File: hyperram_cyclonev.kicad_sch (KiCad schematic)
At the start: 61 parts, among them IC1 AP63205WU, IC2 TXB0108PWR, IC3 S26KL128SDABHI020, IC4 W25Q32JVSSIQ_TR, IC5 S27KL0641DABHI020, J1 ASP-122952-01, J2 HDMI_A, J3 1156915, J4 1156915, J5 Conn_02x06_Top_Bottom, J6 Conn_02x06_Top_Bottom, J7 Conn_02x06_Top_Bottom, J8 1156915, J9 1156915, Q1 BSS138, Q2 BSS138

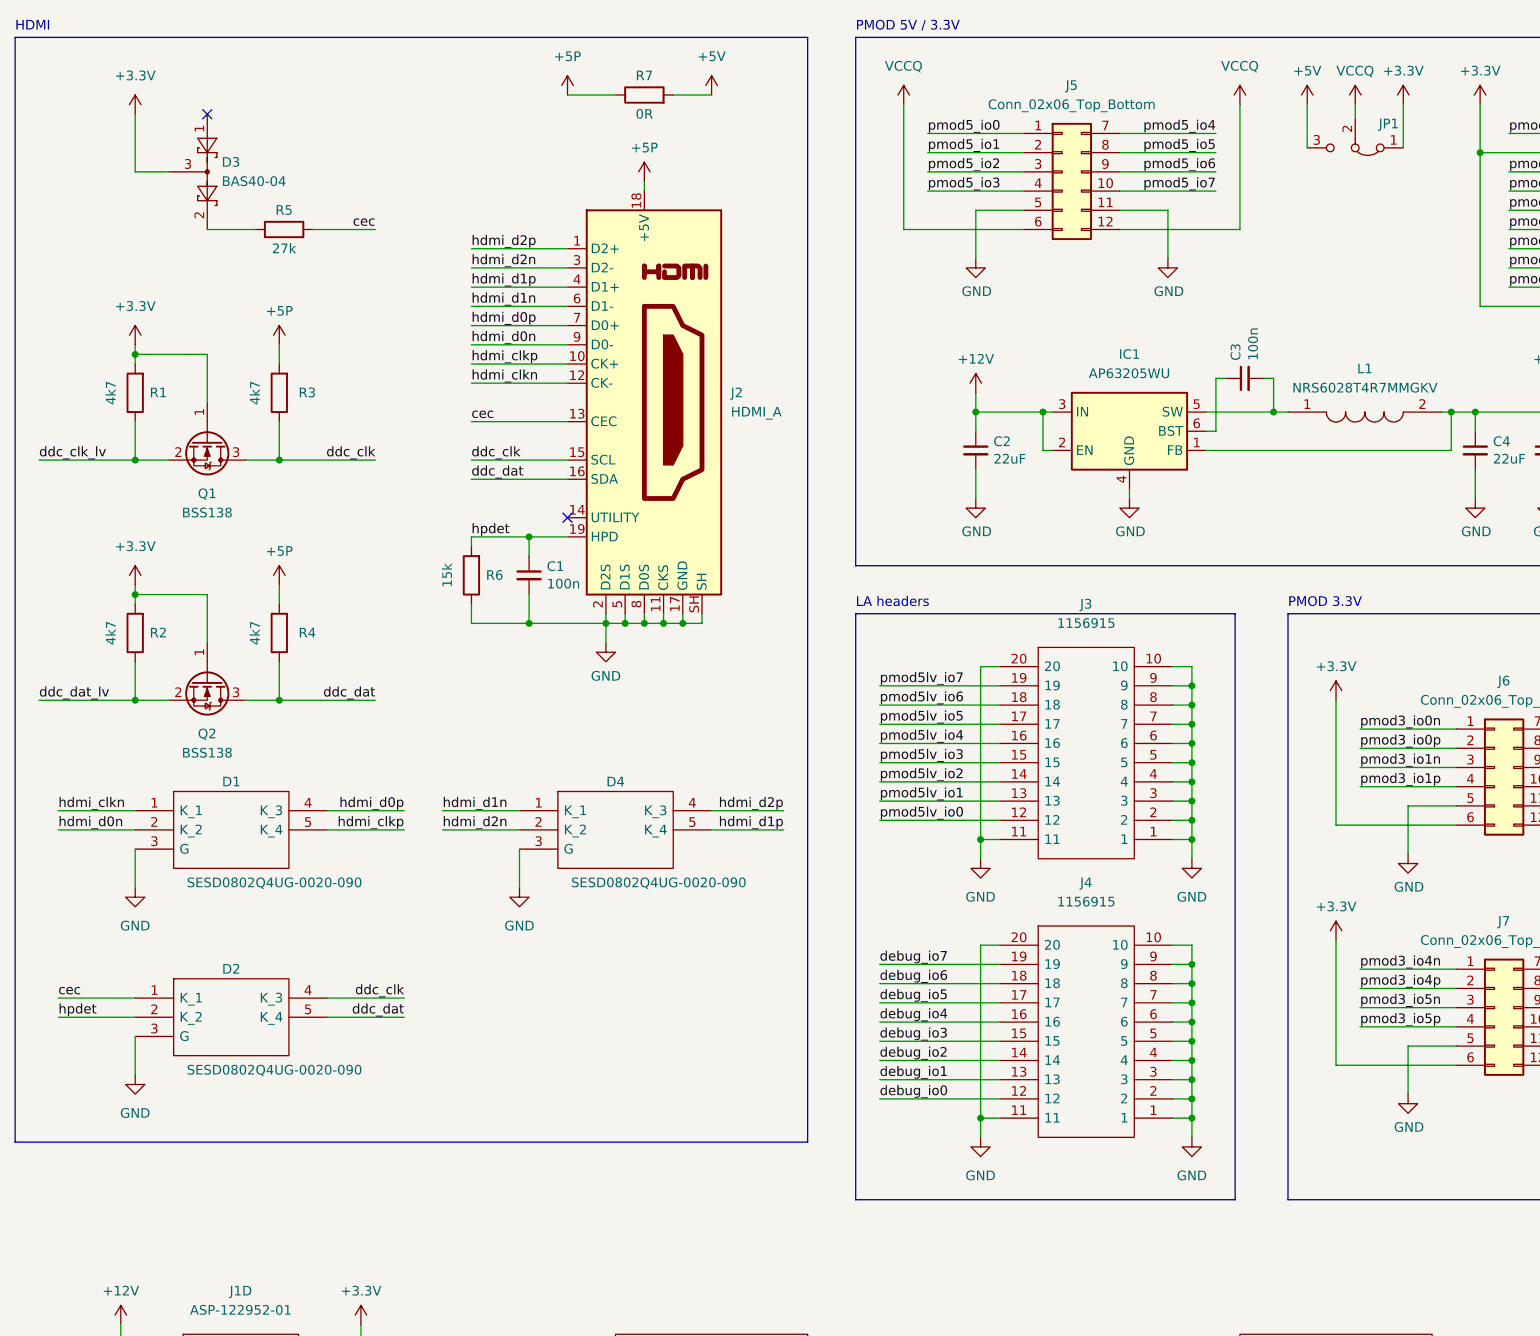
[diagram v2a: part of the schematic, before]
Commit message: Added 100nF capacitors in series for HDMI signals to get TMDS working with LVDS3 outputs on FPGA.
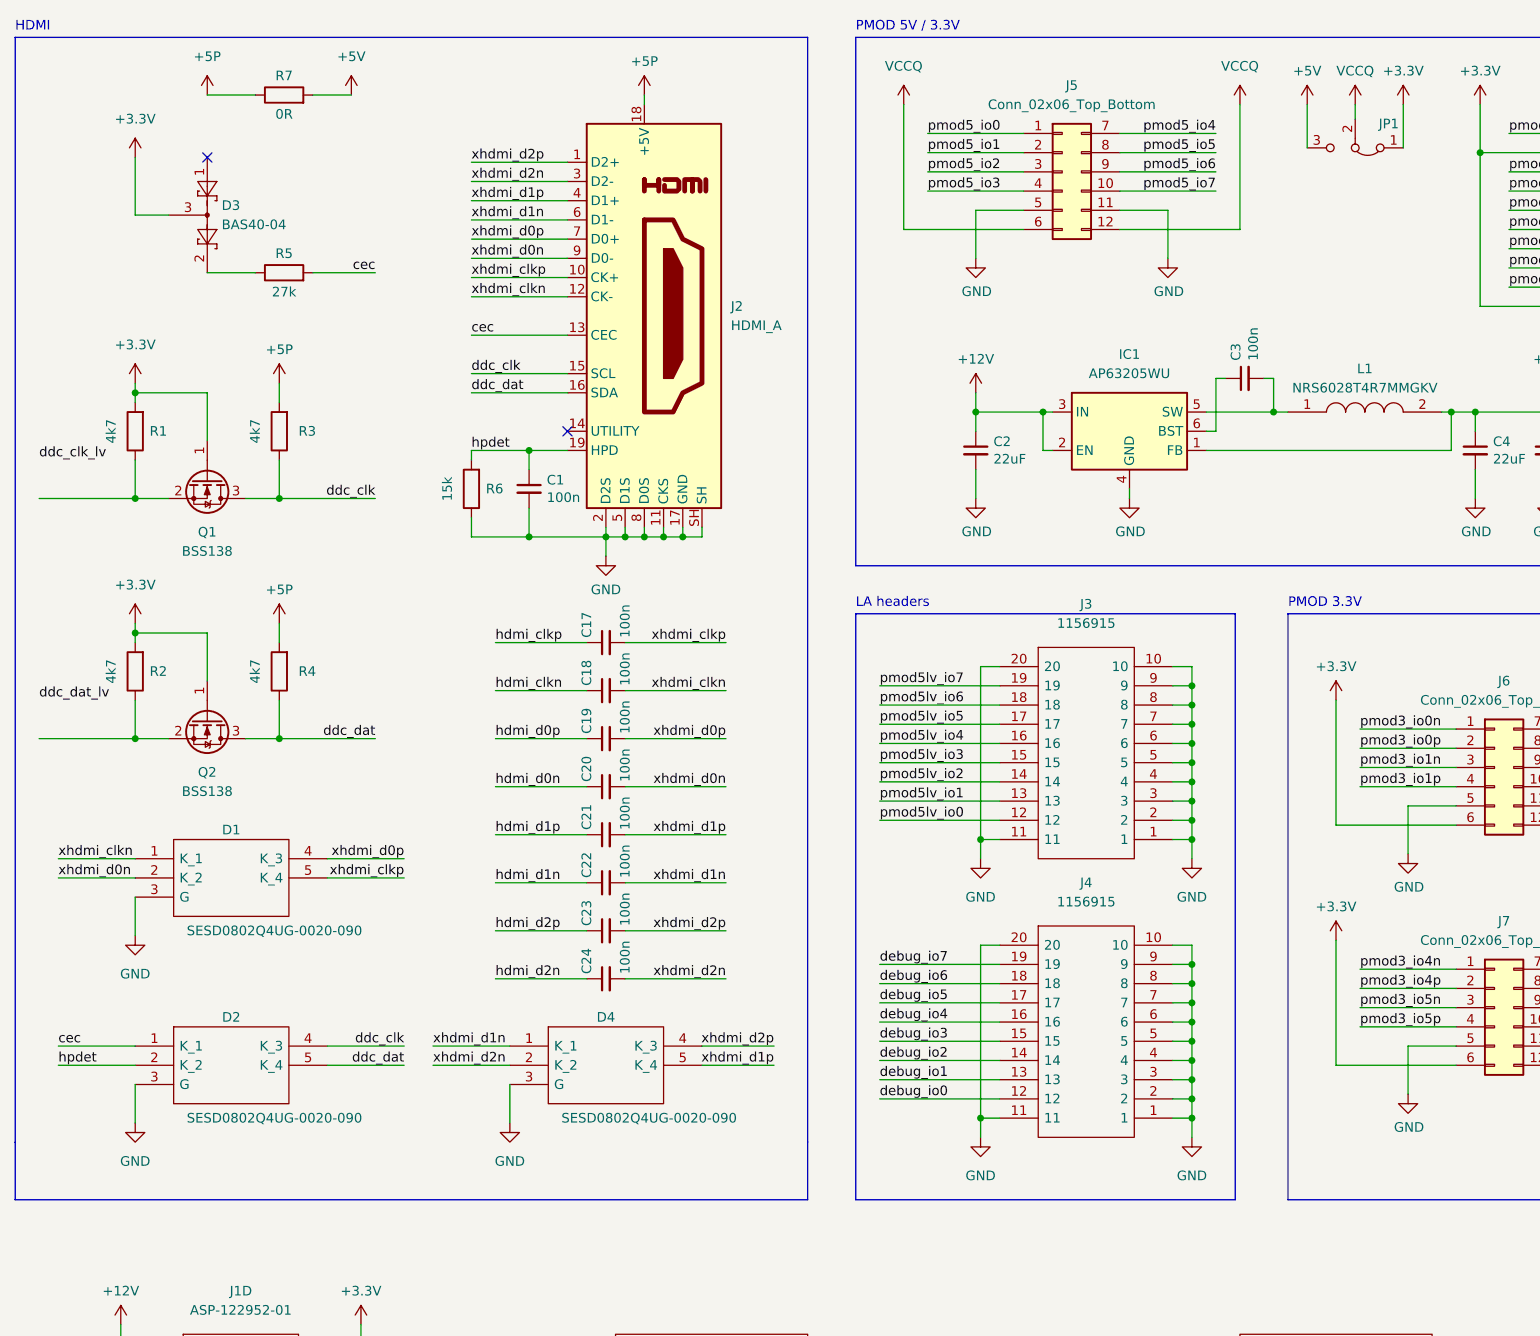
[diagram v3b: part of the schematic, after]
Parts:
- added C17, C18, C19, C20, C21, C22, C23, C24: 100n, Capacitor_SMD:C_0603_1608Metric_Pad1.08x0.95mm_HandSolder, symbol Device:C_Small
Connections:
- net ddc_clk_lv: no longer Q1.2 (S), R1.1
- net ddc_dat_lv: no longer Q2.2 (S), R2.1
- net hdmi_clkn: now also C18.1; no longer D1.1 (K_1), J2.12 (CK-)
- net hdmi_clkp: now also C17.1; no longer D1.5 (K_4), J2.10 (CK+)
- net hdmi_d0n: now also C20.1; no longer D1.2 (K_2), J2.9 (D0-)
- net hdmi_d0p: now also C19.1; no longer D1.4 (K_3), J2.7 (D0+)
- net hdmi_d1n: now also C22.1; no longer D4.1 (K_1), J2.6 (D1-)
- net hdmi_d1p: now also C21.1; no longer D4.5 (K_4), J2.4 (D1+)
- net hdmi_d2n: now also C24.1; no longer D4.2 (K_2), J2.3 (D2-)
- net hdmi_d2p: now also C23.1; no longer D4.4 (K_3), J2.1 (D2+)
- new net: Q1.2 (S), R1.1
- new net: Q2.2 (S), R2.1
- new net xhdmi_clkn: C18.2, D1.1 (K_1), J2.12 (CK-)
- new net xhdmi_clkp: C17.2, D1.5 (K_4), J2.10 (CK+)
- new net xhdmi_d0n: C20.2, D1.2 (K_2), J2.9 (D0-)
- new net xhdmi_d0p: C19.2, D1.4 (K_3), J2.7 (D0+)
- new net xhdmi_d1n: C22.2, D4.1 (K_1), J2.6 (D1-)
- new net xhdmi_d1p: C21.2, D4.5 (K_4), J2.4 (D1+)
- new net xhdmi_d2n: C24.2, D4.2 (K_2), J2.3 (D2-)
- new net xhdmi_d2p: C23.2, D4.4 (K_3), J2.1 (D2+)
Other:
- moved on the sheet: C1, D1, D2, D3, D4, J2, L1, Q1, Q2, R1, R2, R3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

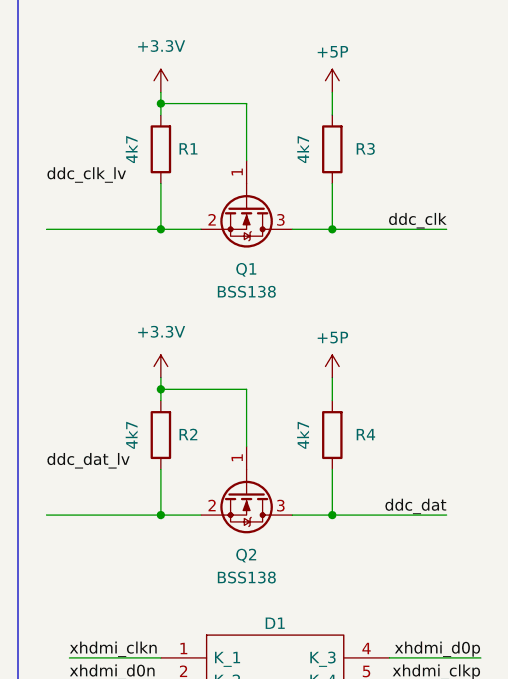
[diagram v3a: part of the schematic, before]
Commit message: Fixed 2 issues with unconnected signals.
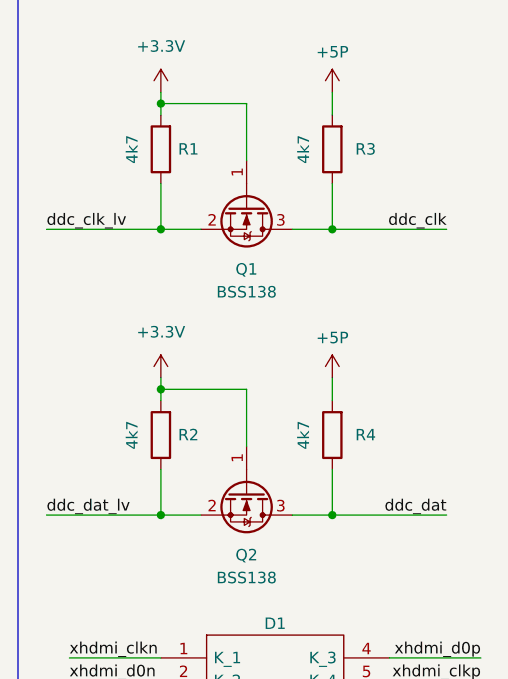
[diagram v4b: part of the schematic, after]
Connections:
- net ddc_clk_lv: now also Q1.2 (S), R1.1
- net ddc_dat_lv: now also Q2.2 (S), R2.1
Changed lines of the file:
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@@
     (effects (font (size 1.27 1.27)) (justify right bottom))
   )
-  (label "ddc_dat_lv" (at 19.05 106.68 0) (fields_autoplaced)
+  (label "ddc_dat_lv" (at 19.05 111.76 0) (fields_autoplaced)
     (effects (font (size 1.27 1.27)) (justify left bottom))
   )
@@
     (effects (font (size 1.27 1.27)) (justify left bottom))
   )
-  (label "ddc_clk_lv" (at 19.05 74.93 0) (fields_autoplaced)
+  (label "ddc_clk_lv" (at 19.05 80.01 0) (fields_autoplaced)
     (effects (font (size 1.27 1.27)) (justify left bottom))
   )
@@
     )
   )
-  (symbol (lib_id "hyperram_cyclonev:ASP-122952-01") (at 58.42 193.04 0) (unit 4)
+  (symbol (lib_name "ASP-122952-01_1") (lib_id "hyperram_cyclonev:ASP-122952-01") (at 58.42 193.04 0) (unit 4)
     (in_bom yes) (on_board yes) (dnp no) (fields_autoplaced)
     (property "Reference" "J1" (at 45.72 184.785 0)

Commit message: Fixed Schematics DRC warnings
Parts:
- Q1, Q2: footprint Package_TO_SOT_SMD:SOT-23_Handsoldering -> Package_TO_SOT_SMD:SOT-23
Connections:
- net GND: now also J3.12, J3.13, J3.14, J3.15, J3.16, J3.17, J3.18, J3.19; no longer J3.2, J3.3, J3.4, J3.5, J3.6, J3.7, J3.8, J3.9
- net pmod5lv_io0: now also J3.2; no longer J3.12
- net pmod5lv_io1: now also J3.3; no longer J3.13
- net pmod5lv_io2: now also J3.4; no longer J3.14
- net pmod5lv_io3: now also J3.5; no longer J3.15
- net pmod5lv_io4: now also J3.6; no longer J3.16
- net pmod5lv_io5: now also J3.7; no longer J3.17
- net pmod5lv_io6: now also J3.8; no longer J3.18
- net pmod5lv_io7: now also J3.9; no longer J3.19
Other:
- moved on the sheet: C2, C3, C4, C5, C6, C7, D1, D2, D3, IC1, J1D, J3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

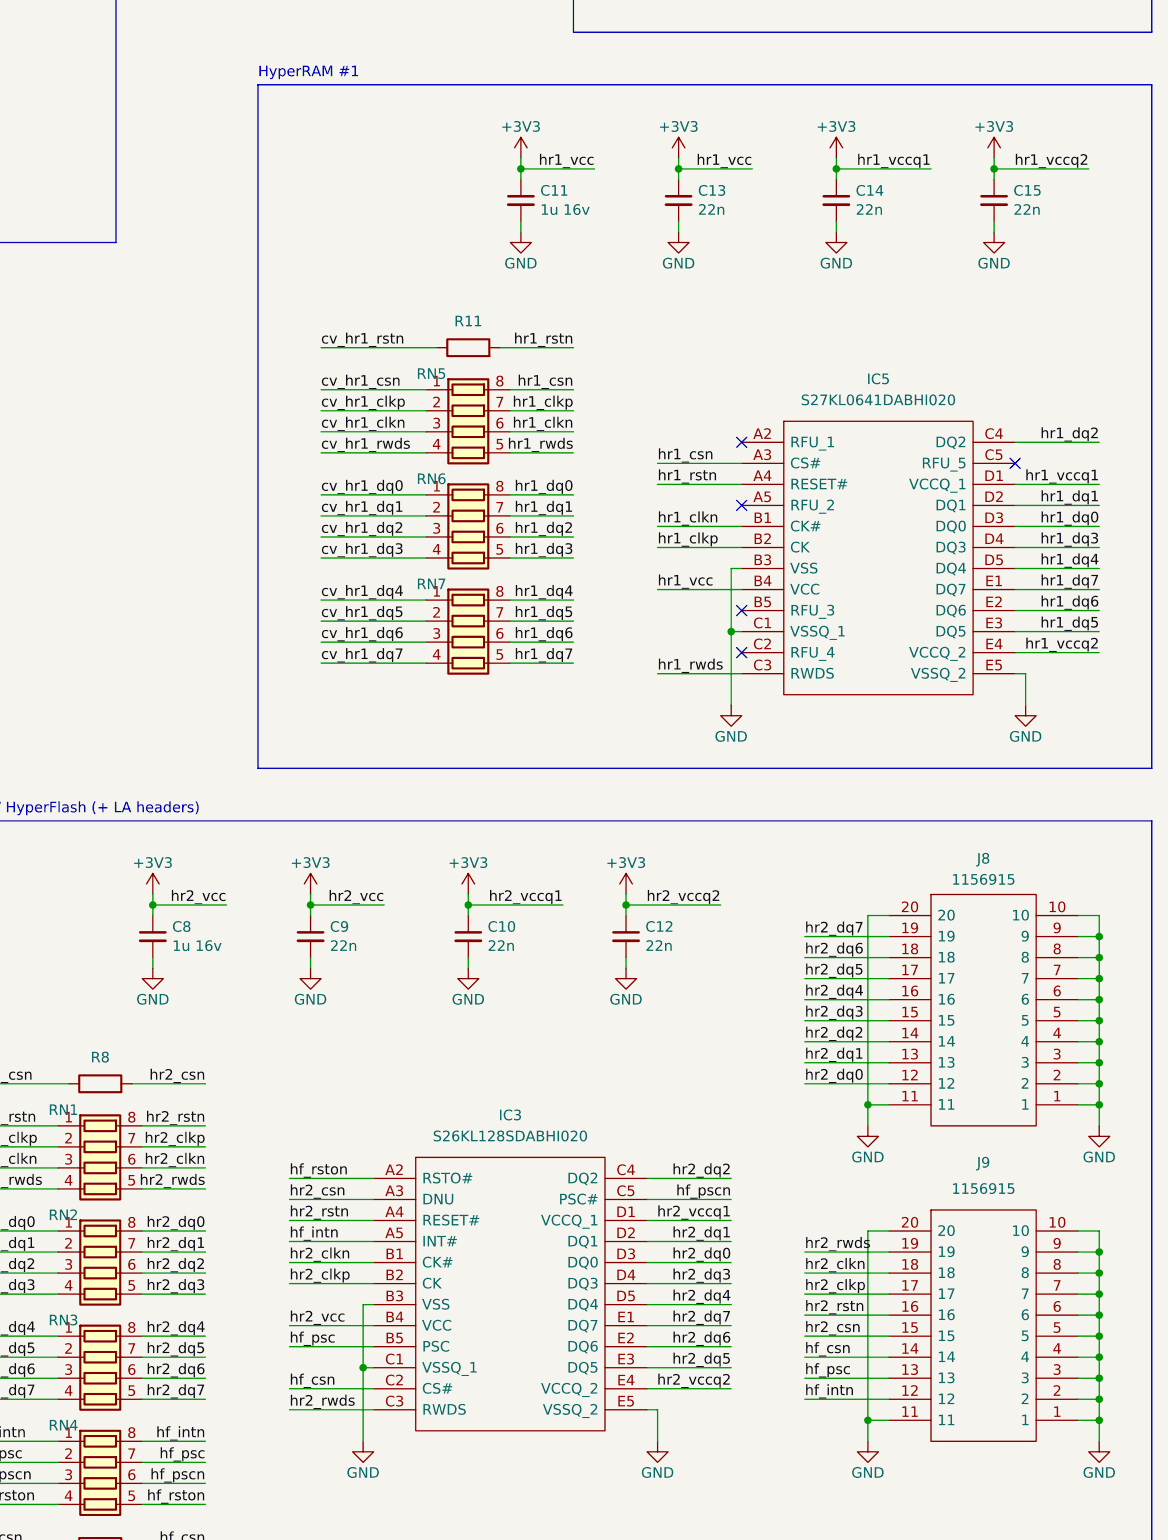
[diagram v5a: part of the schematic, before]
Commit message: Decreased number of ERC complaints. Assigned missing packages.
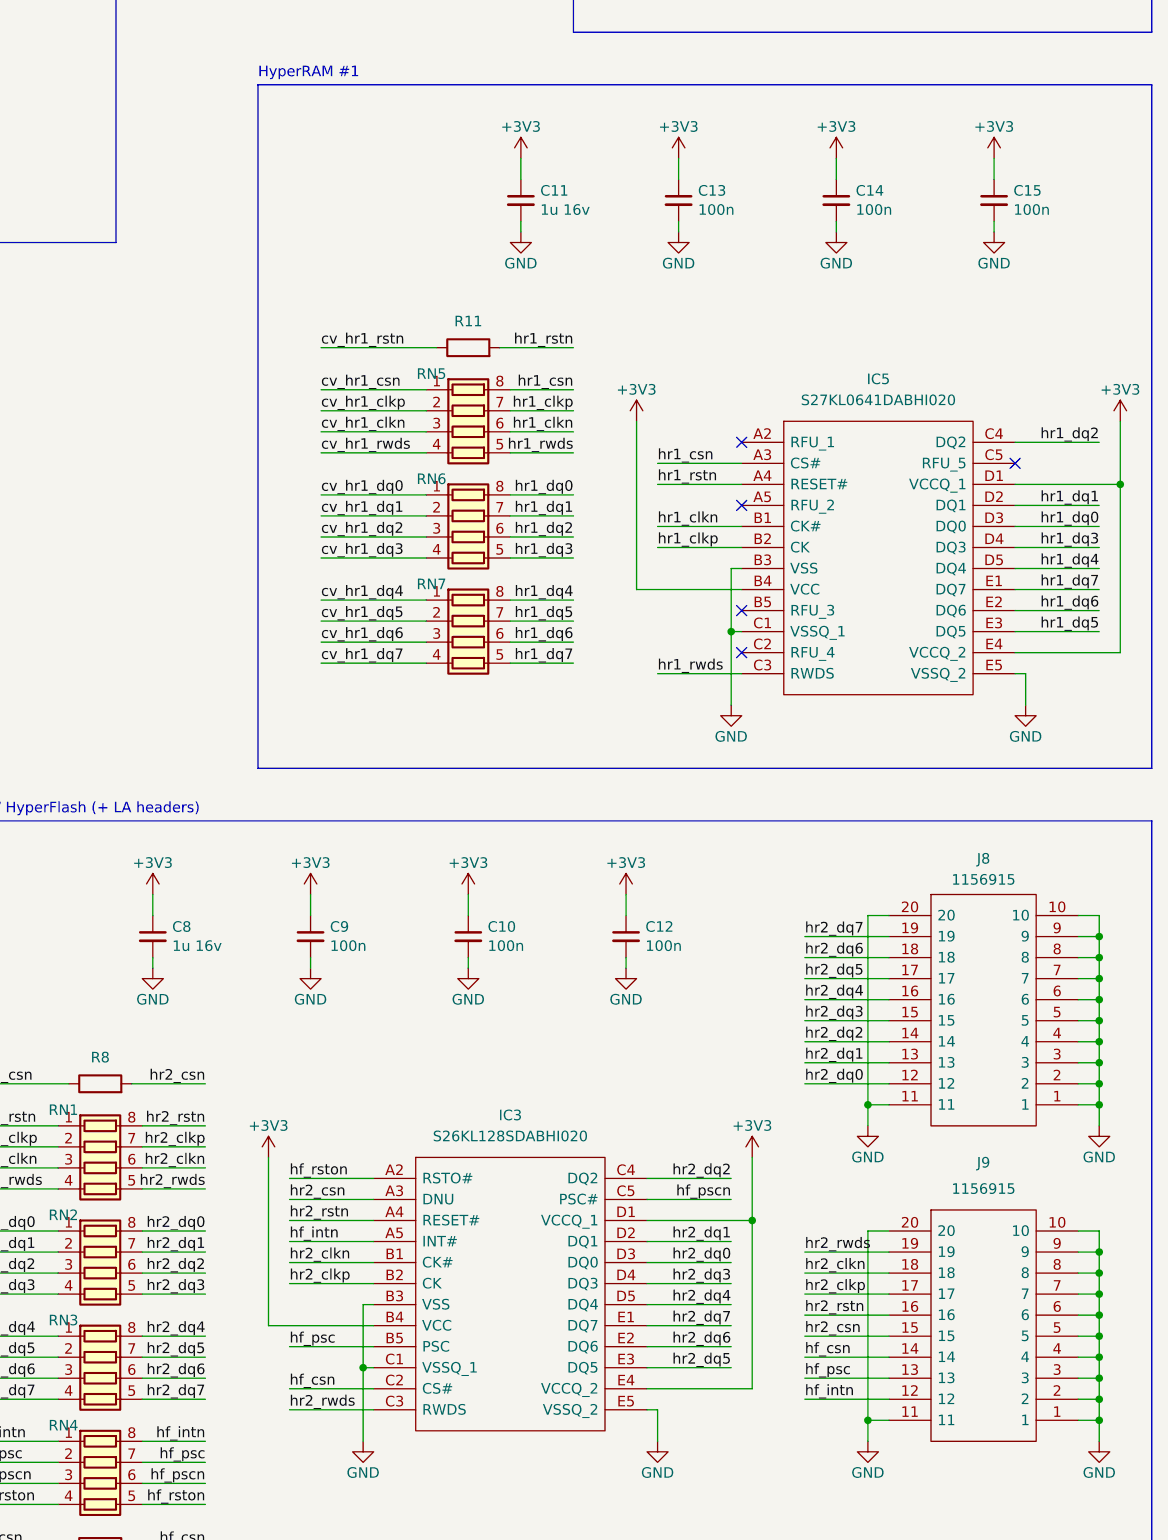
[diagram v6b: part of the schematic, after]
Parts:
- C1, C16: footprint Capacitor_SMD:C_0402_1005Metric_Pad0.74x0.62mm_HandSolder -> Capacitor_SMD:C_0603_1608Metric_Pad1.08x0.95mm_HandSolder
- C10, C12, C13, C14, C15, C9: value 22n -> 100n; footprint Capacitor_SMD:C_0402_1005Metric_Pad0.74x0.62mm_HandSolder -> Capacitor_SMD:C_0603_1608Metric_Pad1.08x0.95mm_HandSolder
- D1, D2, D4: footprint SESD0802Q4UG0020090 -> hyperram_cyclonev:SESD0802Q4UG0020090
- IC2: footprint SOP65P640X120-20N -> hyperram_cyclonev:SOP65P640X120-20N
- IC3, IC5: footprint BGA24C100P5X5_600X800X100 -> hyperram_cyclonev:BGA24C100P5X5_600X800X100
- IC4: footprint SOIC127P790X216-8N -> hyperram_cyclonev:SOIC127P790X216-8N
- J1: footprint ASP12295201 -> hyperram_cyclonev:ASP12295201
- J2: footprint (none) -> hyperram_cyclonev:685119134923
- J3, J4, J8, J9: footprint 1156915 -> hyperram_cyclonev:1156915
- J5, J6, J7: footprint (none) -> hyperram_cyclonev:610112249221
- JP1: footprint (none) -> Connector_PinHeader_2.54mm:PinHeader_1x03_P2.54mm_Vertical
- L1: footprint NRS6028T4R7MMGK -> hyperram_cyclonev:NRS6028T4R7MMGK
- LED1: footprint LEDC2012X80N -> hyperram_cyclonev:LEDC2012X80N
- R1, R10, R11, R2, R3, R4, R5, R6, R7, R8, R9: footprint Resistor_SMD:R_0603_1608Metric -> Resistor_SMD:R_0603_1608Metric_Pad0.98x0.95mm_HandSolder
- RN1, RN2, RN3, RN4, RN5, RN6, RN7: footprint hyperram_asic:CAY16000J4LF -> hyperram_cyclonev:CAY16000J4LF
